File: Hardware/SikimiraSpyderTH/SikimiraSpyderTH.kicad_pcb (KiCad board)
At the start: 2 copper layers, 65.4 x 61.6 mm, 42 parts, among them U1 ESP32_DevKit_V1_DOIT, U3 AMS1117-5.0

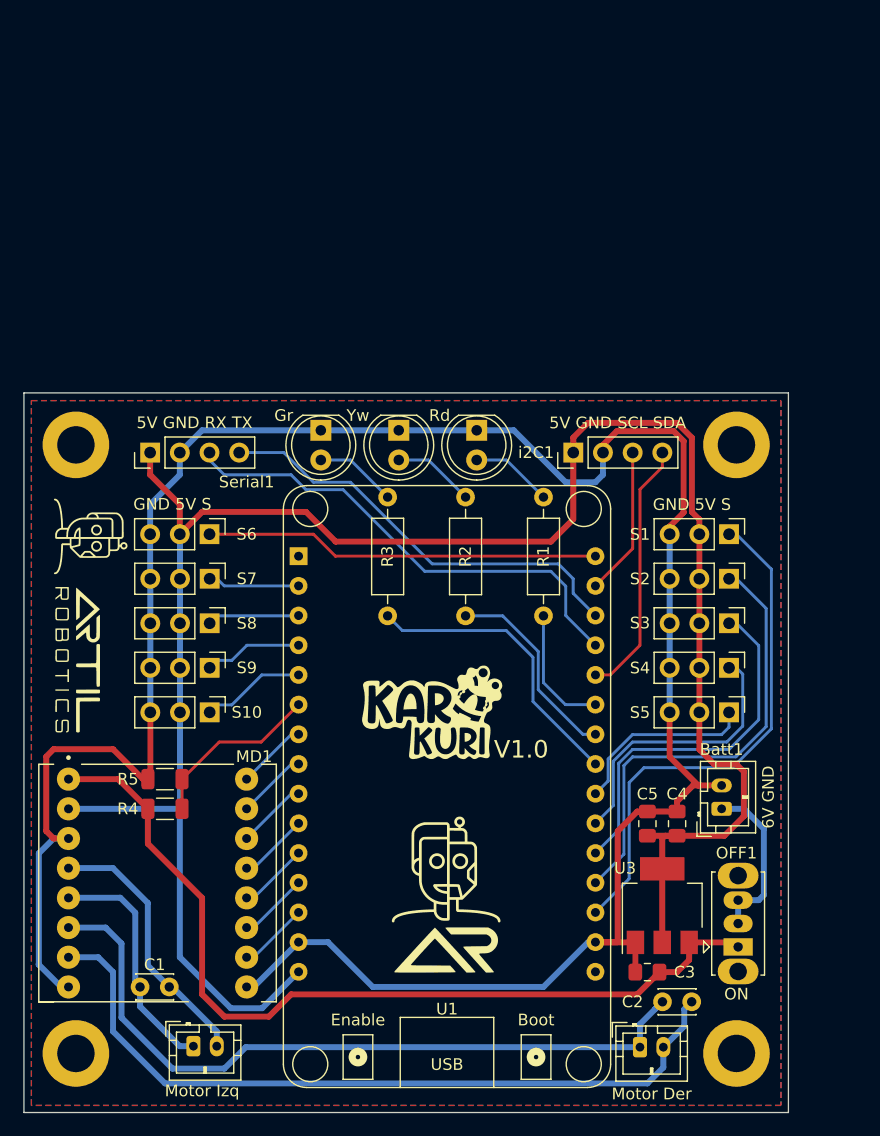
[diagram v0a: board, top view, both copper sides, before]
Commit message: PCB Creada, Cambio de pines
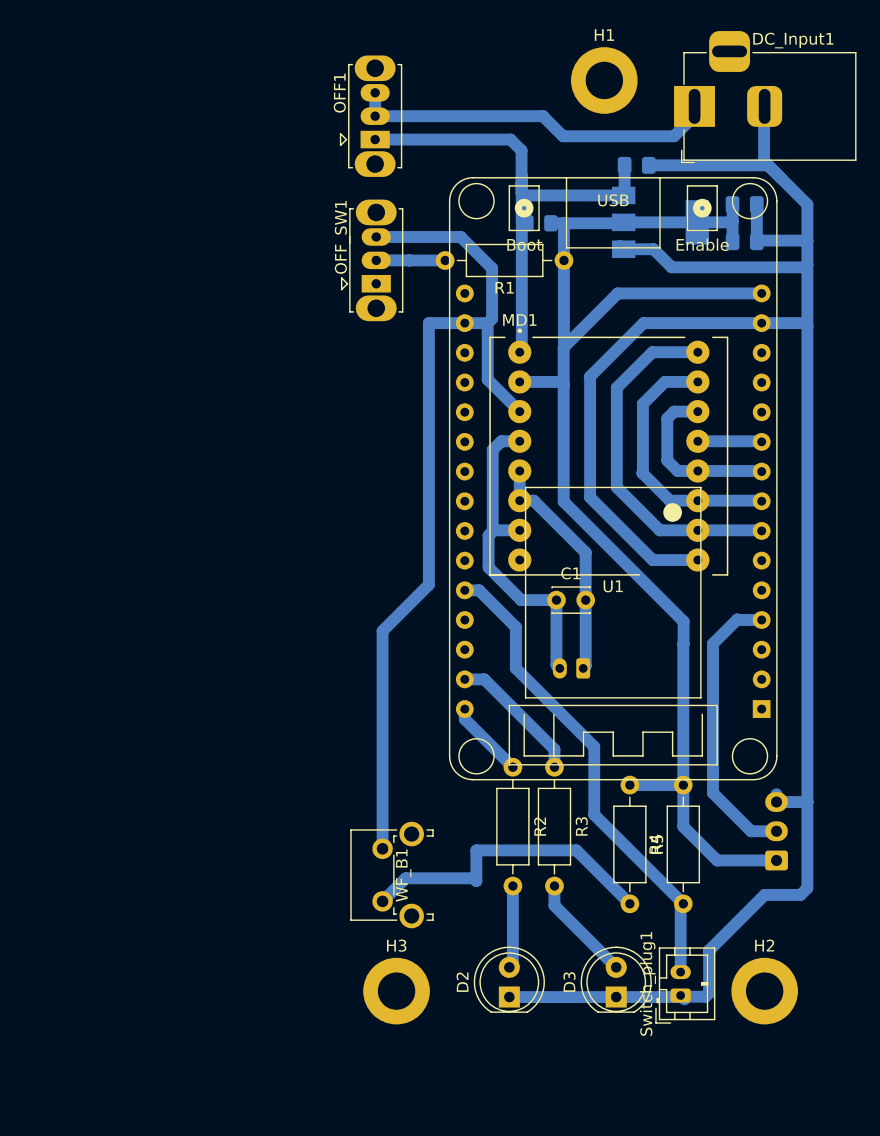
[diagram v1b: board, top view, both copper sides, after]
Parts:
- removed Batt1: 6V GND, Connector_JST:JST_PH_B2B-PH-K_1x02_P2.00mm_Vertical
- removed C2: CAP, Capacitor_THT:C_Disc_D3.0mm_W2.0mm_P2.50mm
- removed G*** (x6): LOGO, LOGO
- removed H4: MountingHole, MountingHole:MountingHole_3.2mm_M3_ISO7380_Pad
- removed M_D1: Motor Der, Connector_JST:JST_PH_B2B-PH-K_1x02_P2.00mm_Vertical
- removed M_I1: Motor Izq, Connector_JST:JST_PH_B2B-PH-K_1x02_P2.00mm_Vertical
- removed S1, S10, S2, S3, S4, S5, S6, S7, S8, S9: GND 5V S, Connector_PinHeader_2.54mm:PinHeader_1x03_P2.54mm_Vertical
- removed Serial1: 5V GND RX TX, Connector_PinHeader_2.54mm:PinHeader_1x04_P2.54mm_Vertical
- removed i2C1: 5V GND SCL SDA, Connector_PinHeader_2.54mm:PinHeader_1x04_P2.54mm_Vertical
- added DC_Input1: Jack-DC, Connector_BarrelJack:BarrelJack_Horizontal, F.Cu at (129.1, 75.2)
- added ENC1: Encoder_plug, Connector_JST:JST_EH_B3B-EH-A_1x03_P2.50mm_Vertical, B.Cu at (136.1, 139.7)
- added M+1: M-, Connector_JST:JST_PH_B2B-PH-K_1x02_P2.00mm_Vertical, B.Cu at (119.6, 123.3)
- added OFF_SW1: ON_SW, Button_Switch_THT:SW_Slide_1P2T_CK_OS102011MS2Q, F.Cu at (101.9, 90.4)
- added Switch_plug1: SW, Connector_JST:JST_PH_B2B-PH-K_1x02_P2.00mm_Vertical, F.Cu at (127.9, 151.3)
- added WF_B1: SW_WF, Button_Switch_THT:SW_Tactile_SPST_Angled_PTS645Vx39-2LFS, F.Cu at (102.4, 143.2)
- C3, C4, C5, U3: moved to B.Cu
- D1: value Rd -> DIODE; footprint LED_THT:LED_D5.0mm -> Diode_SMD:D_0805_2012Metric_Pad1.15x1.40mm_HandSolder; moved to B.Cu
- MD1: footprint TB6612FNG Motor:MODULE_TB6612FNG Motor -> TB6612FNG:MODULE_TB6612FNG Motor
- R4: value 6,2K -> 82; footprint Resistor_SMD:R_1206_3216Metric -> Resistor_THT:R_Axial_DIN0207_L6.3mm_D2.5mm_P10.16mm_Horizontal
- R5: value 3,6K -> 82; footprint Resistor_SMD:R_1206_3216Metric -> Resistor_THT:R_Axial_DIN0207_L6.3mm_D2.5mm_P10.16mm_Horizontal
- U1: footprint esp32_devkit_v1_doit:esp32_devkit_v1_doit -> ESP32_30PIN:esp32_devkit_v1_doit
- moved OFF1 75.7 mm to (101.8, 78.0)
- moved C3 69.0 mm to (124.2, 80.2), turned to 0 degrees
- moved U3 58.5 mm to (126.2, 85.1), turned to 0 degrees
- moved H1 54.9 mm to (121.4, 73.0)
- moved D3 54.7 mm to (122.4, 151.4), turned to 90 degrees
- moved C4 53.3 mm to (133.4, 83.6), turned to 0 degrees
- moved MD1 53.1 mm to (121.8, 105.1)
- moved C5 50.5 mm to (133.4, 86.8), turned to 0 degrees
- moved D2 49.4 mm to (113.3, 151.4), turned to 90 degrees
- moved C1 46.8 mm to (117.3, 117.4), turned to 0 degrees
- moved H2 46.8 mm to (135.1, 150.9)
- moved R4 45.1 mm to (128.2, 143.4), turned to 90 degrees
- moved R5 39.8 mm to (123.6, 133.2), turned to -90 degrees
- moved R1 30.5 mm to (118.0, 88.4), turned to 180 degrees
- moved H3 27.9 mm to (103.6, 150.9)
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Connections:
- C1 pad 1: M_L+ -> M+
- C1 pad 2: M_L- -> M-
- D1 pad 1: GND -> +5V
- D1 pad 2: Net-(D1-Pad2) -> +BATT
- MD1 pad 10: /PWMB -> /PWMA
- MD1 pad 11: /BI2 -> /AI2
- MD1 pad 12: /BI1 -> /AI1
- MD1 pad 4: M_L+ -> M+
- MD1 pad 5: M_L- -> M-
- MD1 pad 6: M_R- -> M-
- MD1 pad 7: M_R+ -> M+
- R1 pad 1: /Lrojo -> +5V
- R1 pad 2: Net-(D1-Pad2) -> /Switch
- R2 pad 1: /Lamarillo -> /LedAct
- R3 pad 1: /Lverde -> /LedWifi
- R4 pad 1: /BM -> /EndSwitch
- R4 pad 2: +BATT -> +5V
- R5 pad 1: GND -> +5V
- R5 pad 2: /BM -> /WF_Button
- U1 pad 1: /EN -> unconnected-(U1-Pad1)
- U1 pad 11: /BI1 -> unconnected-(U1-Pad11)
- U1 pad 12: /BI2 -> unconnected-(U1-Pad12)
- U1 pad 13: /PWMB -> unconnected-(U1-Pad13)
- U1 pad 18: /S1 -> unconnected-(U1-Pad18)
- U1 pad 19: /S2 -> unconnected-(U1-Pad19)
- U1 pad 2: /S7 -> unconnected-(U1-Pad2)
- U1 pad 20: /S3 -> unconnected-(U1-Pad20)
- U1 pad 21: /S4 -> unconnected-(U1-Pad21)
- U1 pad 22: /S5 -> unconnected-(U1-Pad22)
- U1 pad 23: /Lverde -> unconnected-(U1-Pad23)
- U1 pad 24: /Lamarillo -> unconnected-(U1-Pad24)
- U1 pad 25: /Lrojo -> unconnected-(U1-Pad25)
- U1 pad 26: /SDA -> /EndSwitch
- U1 pad 27: /RX -> unconnected-(U1-Pad27)
- U1 pad 28: /TX -> unconnected-(U1-Pad28)
- U1 pad 29: /SCL -> /LedWifi
- U1 pad 3: /S8 -> unconnected-(U1-Pad3)
- U1 pad 30: /S6 -> /LedAct
- U1 pad 4: /S9 -> /Encoder
- U1 pad 5: /S10 -> unconnected-(U1-Pad5)
- U1 pad 6: /BM -> unconnected-(U1-Pad6)
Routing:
- net M_R+: track 65.5 -> 0.00 mm
- net +5V: track 176.3 -> 111.1 mm
- net M_R-: track 63.1 -> 0.00 mm
- net GND: track 205.0 -> 258.0 mm
- net /S1: track 45.2 -> 0.00 mm
- net /RX: track 41.7 -> 0.00 mm
- net /EndSwitch: track 0.00 -> 41.2 mm
- net /S2: track 39.2 -> 0.00 mm
- net /TX: track 37.0 -> 0.00 mm
- net /S6: track 33.8 -> 0.00 mm
- net /S3: track 32.0 -> 0.00 mm
- net +BATT: track 76.0 -> 46.5 mm
- net M+: track 0.00 -> 28.0 mm
- net /WF_Button: track 0.00 -> 26.6 mm
- net /Lverde: track 25.2 -> 0.00 mm
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- removed copper zone on F.Cu, net +5V
- removed copper zone on B.Cu, net GND
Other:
- board outline removed
- board text removed: "V1.0"

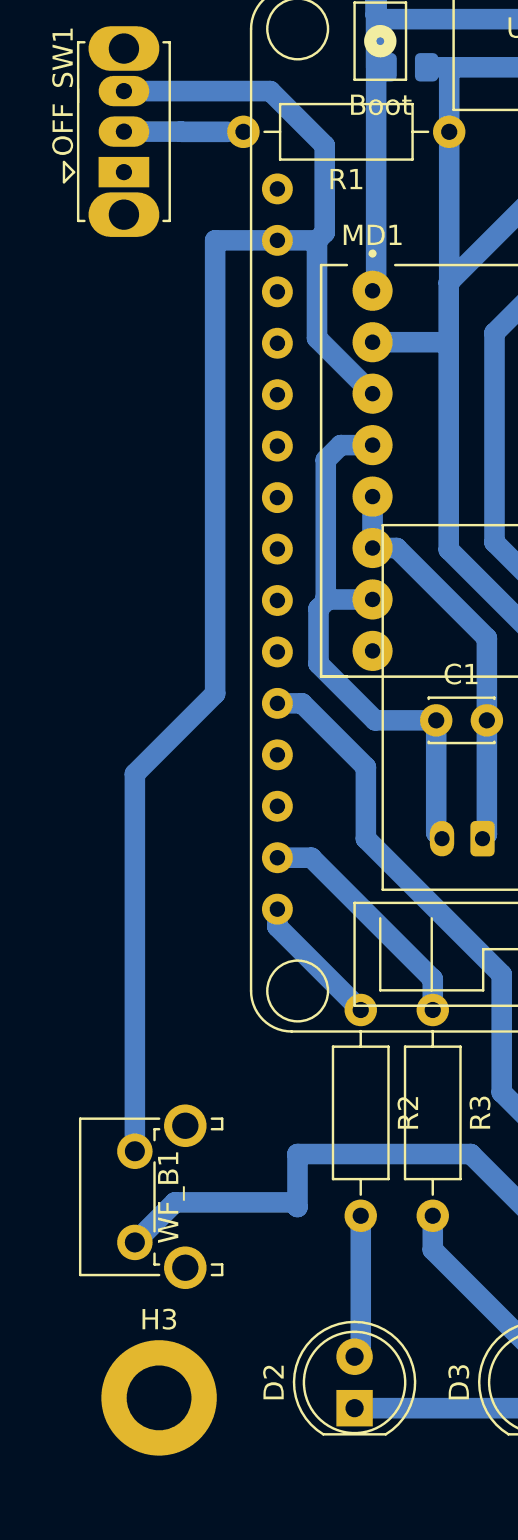
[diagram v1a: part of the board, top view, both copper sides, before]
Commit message: Cambiado de pines y corregido PCB
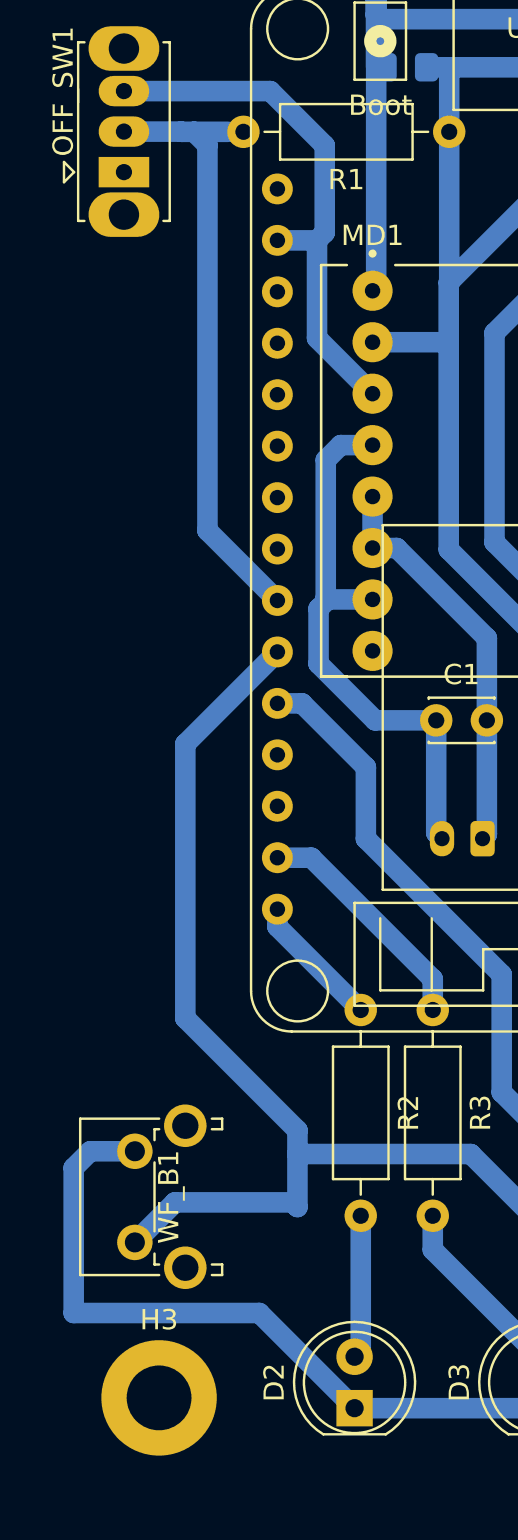
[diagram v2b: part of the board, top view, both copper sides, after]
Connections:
- OFF_SW1 pad 2: /Switch -> /Demo_SW
- R1 pad 2: /Switch -> /Demo_SW
- U1 pad 24: unconnected-(U1-Pad24) -> /Demo_SW
- U1 pad 25: unconnected-(U1-Pad25) -> /WF_Button
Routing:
- net /Demo_SW: track 0.00 -> 30.0 mm
- net /WF_Button: track 26.6 -> 55.5 mm
- net GND: track 258.0 -> 234.7 mm
- net /Switch: track 5.14 -> 0.00 mm

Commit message: Pcbs Update
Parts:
- M+1: footprint Connector_JST:JST_PH_B2B-PH-K_1x02_P2.00mm_Vertical -> TerminalBlock:TerminalBlock_bornier-2_P5.08mm
- moved M+1 1.67 mm to (119.1, 121.7)
- moved R3 1.54 mm to (117.3, 133.2)
- moved R2 1.52 mm to (113.5, 133.2)
- moved D2 0.25 mm to (113.5, 151.4)
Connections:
- U1 pad 11: unconnected-(U1-Pad11) -> /Encoder
- U1 pad 4: /Encoder -> unconnected-(U1-Pad4)
- WF_B1 pad 1: /WF_Button -> GND
- WF_B1 pad 2: GND -> /WF_Button
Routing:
- net GND: track 234.7 -> 209.7 mm
- net /Encoder: track 24.6 -> 43.3 mm
- net /EndSwitch: track 41.2 -> 49.3 mm
- net +BATT: track 46.5 -> 52.3 mm
- net Net-(DC_Input1-Pad1): track 30.7 -> 35.1 mm
- net M+: track 28.0 -> 26.3 mm
- net +5V: track 111.1 -> 109.4 mm
- net Net-(D3-Pad2): track 9.15 -> 7.54 mm
- net /LedWifi: track 11.7 -> 13.3 mm
- net Net-(D2-Pad2): track 7.09 -> 5.58 mm
- net /LedAct: track 6.68 -> 8.19 mm
- net /Demo_SW: track 30.0 -> 31.0 mm
- added copper zone on B.Cu, net GND
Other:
- board text added: "Artil_Sikimira-V1.0"
